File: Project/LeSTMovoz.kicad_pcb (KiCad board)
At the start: 2 copper layers, 242.9 x 76.2 mm, 122 parts, among them J1 USB_C_Receptacle_USB2.0, SW1 SKQGABE010, U1 STM32F072RBTx, U2 L78L33_TO92, U3 74AHCT1G125

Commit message: fresh gerbers
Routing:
- net GND: track 86.9 -> 88.6 mm, vias 15 -> 22
- net VBUS: track 112.7 -> 112.1 mm
- net +5V: track 81.3 -> 81.8 mm

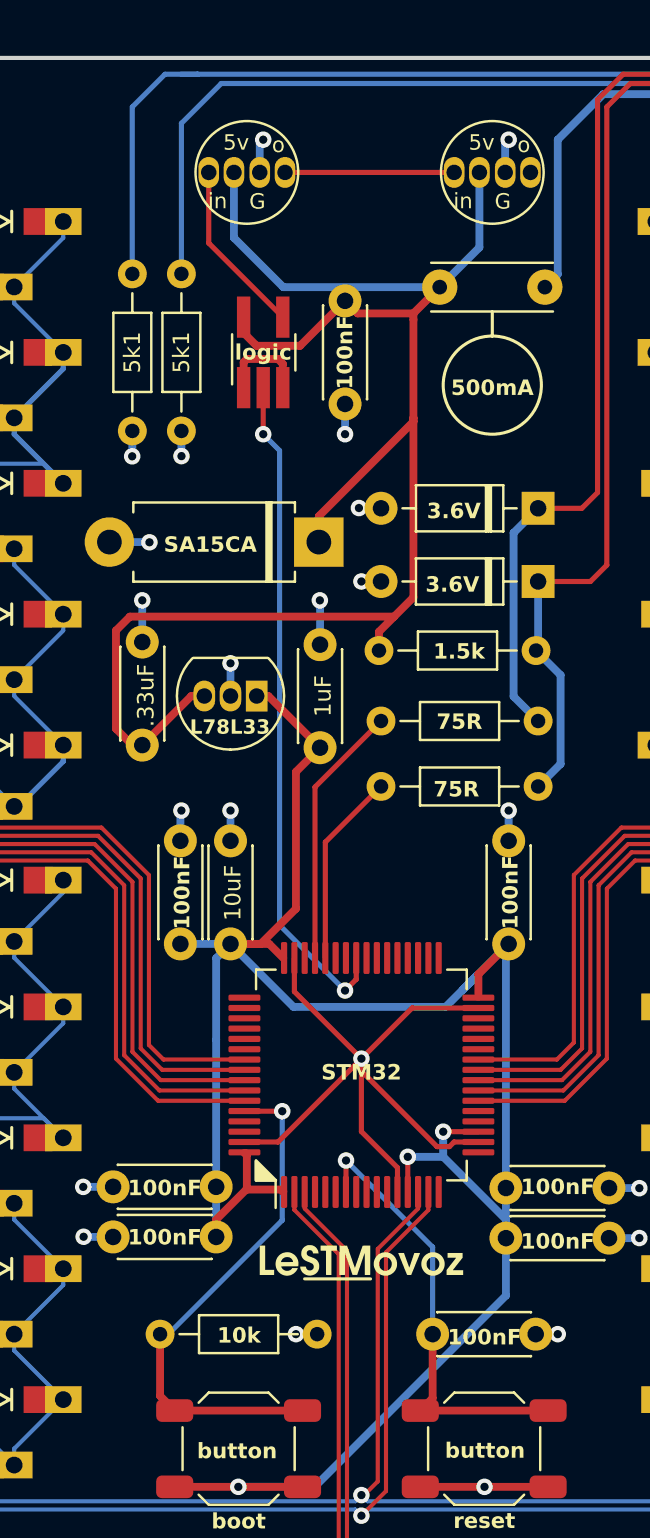
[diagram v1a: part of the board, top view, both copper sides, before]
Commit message: changed rgb component, 10k for 2*5k1 resistors, finished THT BOM
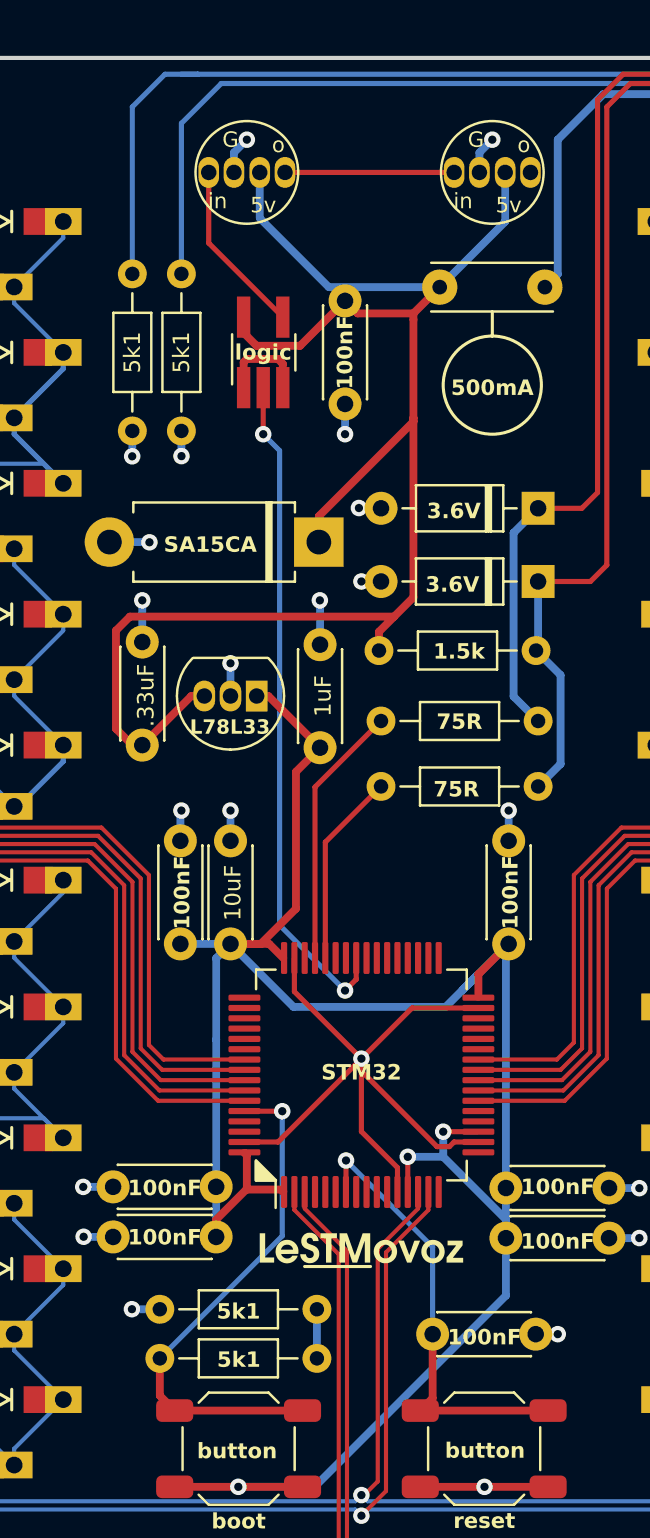
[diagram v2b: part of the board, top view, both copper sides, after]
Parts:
- added R7: 5k1, Resistor_THT:R_Axial_DIN0204_L3.6mm_D1.6mm_P7.62mm_Horizontal, F.Cu at (135.5, 84.5)
- D44, D45: value WS2812B -> WS2812D-F5
- R6: value 10k -> 5k1
- moved R6 1.17 mm to (135.5, 86.9)
- moved G*** 0.60 mm to (145.3, 81.5)
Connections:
- D44 pad 1: +5V -> GND
- D44 pad 3: GND -> +5V
- D45 pad 1: +5V -> GND
- D45 pad 3: GND -> +5V
- R6 pad 2: GND -> Net-(R6-Pad2)
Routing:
- net Net-(R6-Pad2): track 0.00 -> 2.38 mm
- net +5V: track 81.8 -> 80.5 mm
- net GND: track 88.6 -> 89.3 mm
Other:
- board text removed: "10k"
